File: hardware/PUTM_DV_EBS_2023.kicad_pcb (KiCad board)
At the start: 4 copper layers, 100 x 70 mm, 155 parts, among them IC1 UCC2946DG4, J1 SAFETY_SUPPLY, J2 SWDIO_CONN, J3 SENSORS, J4 VALVES, J5 MAIN, K1 FINDER-30.22, K2 FINDER-30.22, Q1 BSS123, Q2 BSS123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

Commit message: 2.0 layot wip, each sections placed
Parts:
- removed D10: UDZV_3.3B, Diode_SMD:D_SOD-323_HandSoldering
- removed the R11 at (150.6, 42.7)
- removed R25: 2.2k, Resistor_SMD:R_0603_1608Metric_Pad0.98x0.95mm_HandSolder
- removed the R5 at (43.2, 33.5)
- removed the R5 at (59.7, 58.9)
- removed the R7 at (74.3, 77.5)
- added JP2: Jumper_NC_Small, Jumper:SolderJumper-2_P1.3mm_Open_RoundedPad1.0x1.5mm, F.Cu at (124.8, 154.6)
- added JP3: Jumper_NC_Small, Jumper:SolderJumper-2_P1.3mm_Open_RoundedPad1.0x1.5mm, F.Cu at (124.8, 158.1)
- added R5: 100R, Resistor_SMD:R_0603_1608Metric_Pad0.98x0.95mm_HandSolder, F.Cu at (152.2, 116.3)
- 120_JP1: footprint Connector_PinHeader_2.54mm:PinHeader_1x02_P2.54mm_Vertical -> Jumper:SolderJumper-2_P1.3mm_Open_RoundedPad1.0x1.5mm
- R11, R2, R33, R6: value 2.2k -> 100R
- moved C30 145.2 mm to (175.1, 125.1)
- moved D13 142.6 mm to (174.9, 127.0)
- moved R30 141.2 mm to (171.8, 125.1)
- moved C29 135.3 mm to (157.5, 125.3)
- moved D14 133.1 mm to (157.2, 132.2)
- moved D9 133.1 mm to (157.2, 127.3)
- moved R28 131.2 mm to (154.2, 125.3)
- moved R6 130.1 mm to (152.2, 110.2)
- moved R11 127.9 mm to (152.2, 108.7)
- moved R33 126.9 mm to (152.2, 111.8)
- moved R49 121.8 mm to (145.7, 115.1)
- moved R29 121.8 mm to (145.7, 110.1)
- moved R50 121.8 mm to (145.7, 117.6)
- moved R14 116.2 mm to (162.7, 108.2)
- moved R16 116.2 mm to (162.7, 106.7)
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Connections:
- U5 pad 26: SPARE1 -> Net-(JP2-A)
- U5 pad 27: SPARE2 -> Net-(JP3-B)
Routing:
- net SPARE2: track 7.06 -> 0.00 mm, vias 2 -> 0
- net Net-(JP3-B): track 0.00 -> 7.06 mm, vias 0 -> 2
- net SPARE1: track 6.13 -> 0.00 mm
- net Net-(JP2-A): track 0.00 -> 6.13 mm
- net /EBS Logic/SAFETY_IN: track 5.07 -> 0.00 mm
- net /Input Protection/SAFETY_SENSE_P: track 0.00 -> 3.60 mm
- net GND: track 51.0 -> 49.4 mm
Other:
- board text added: "SDC_K_CTRL"
- board text added: "Test points:"
- board text added: "WD_RDY"
- board text removed: "AND2"
- board text removed: "LATCH_CHK"
- board text removed: "NAND1"
- board text removed: "RST_EBS"
- board text removed: "RST_LATCH"
- board text removed: "RTH"
- board text removed: "SDC_K"

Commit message: WIP 1.1 routing
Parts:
- removed the C27 at (140.8, 142.9)
- removed JP3: Jumper_NC_Small, Jumper:SolderJumper-2_P1.3mm_Open_RoundedPad1.0x1.5mm
- removed Q1: BSS123, Package_TO_SOT_SMD:SOT-23
- added JP1: Jumper_NC_Small, Jumper:SolderJumper-2_P1.3mm_Open_RoundedPad1.0x1.5mm, F.Cu at (128.6, 82.8)
- added REF**: PinHeader_2x06_P2.54mm_Vertical, Connector_PinHeader_2.54mm:PinHeader_2x06_P2.54mm_Vertical, F.Cu at (172.8, 75.6)
- R1: value 1k -> 100R
- R20, R4: value 2.2k -> 100R
- moved R49 97.7 mm to (57.3, 73.4)
- moved R29 96.5 mm to (57.3, 71.4)
- moved R50 96.5 mm to (57.3, 78.9)
- moved 120_JP1 86.8 mm to (120.1, 44.2), turned to 0 degrees
- moved R13 84.8 mm to (120.7, 47.1), turned to -90 degrees
- moved JP2 74.4 mm to (128.6, 80.3), turned to 180 degrees
- moved C14 71.3 mm to (120.5, 63.9), turned to -90 degrees
- moved C15 67.6 mm to (118.9, 65.7)
- moved U6 65.8 mm to (115.3, 65.7), turned to 90 degrees
- moved C23 63.0 mm to (147.1, 74.0)
- moved C27 63.0 mm to (151.7, 74.0)
- moved U10 63.0 mm to (154.0, 74.8)
- moved U8 63.0 mm to (144.8, 74.8)
- moved U9 63.0 mm to (149.4, 74.8)
- moved C4 63.0 mm to (142.3, 74.0)
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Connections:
- JP2 pad 1: Net-(JP2-A) -> SPARE2
- JP2 pad 2: SPARE1 -> Net-(JP2-B)
- R11 pad 1: Net-(U5-PB4) -> Net-(U5-PB0)
- R5 pad 1: Net-(U5-PB5) -> Net-(U5-PB1)
- R6 pad 1: Net-(U5-PB6) -> Net-(U5-PB2)
- U5 pad 24: unconnected-(U5-PC4-Pad24) -> Net-(JP1-A)
- U5 pad 25: unconnected-(U5-PC5-Pad25) -> Net-(JP2-B)
- U5 pad 26: Net-(JP2-A) -> Net-(U5-PB0)
- U5 pad 27: Net-(JP3-B) -> Net-(U5-PB1)
- U5 pad 28: unconnected-(U5-PB2-Pad28) -> Net-(U5-PB2)
- U5 pad 56: Net-(U5-PB4) -> unconnected-(U5-PB4-Pad56)
- U5 pad 57: Net-(U5-PB5) -> unconnected-(U5-PB5-Pad57)
- U5 pad 58: Net-(U5-PB6) -> unconnected-(U5-PB6-Pad58)
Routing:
- net EBS_RESET _BUTTON: track 43.5 -> 0.00 mm, vias 4 -> 0
- net /Air pressure sensor control/PRESS4: track 0.00 -> 15.1 mm
- net Net-(Q2-G): track 31.4 -> 18.8 mm
- net /EBS Supervisor/VALVE_2: track 0.00 -> 11.2 mm
- net Net-(Q3-G): track 44.3 -> 34.3 mm
- net +3V3: track 86.3 -> 78.2 mm, vias 32 -> 22
- net Net-(U4--): track 0.00 -> 7.55 mm
- net Net-(U2--): track 0.00 -> 7.55 mm
- net Net-(U1--): track 0.00 -> 7.55 mm
- net Net-(U3--): track 0.00 -> 7.55 mm
- net Net-(JP3-B): track 7.06 -> 0.00 mm, vias 2 -> 0
- net CAN+: track 0.00 -> 6.75 mm
- net Net-(JP2-A): track 6.13 -> 0.00 mm
- net Net-(IC1-Pad2): track 6.03 -> 0.00 mm
- net CAN-: track 0.00 -> 5.96 mm
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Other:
- board text removed: "///// REROUTE AND REPAIR CRYSTAL"
- board text removed: "Power Supply"

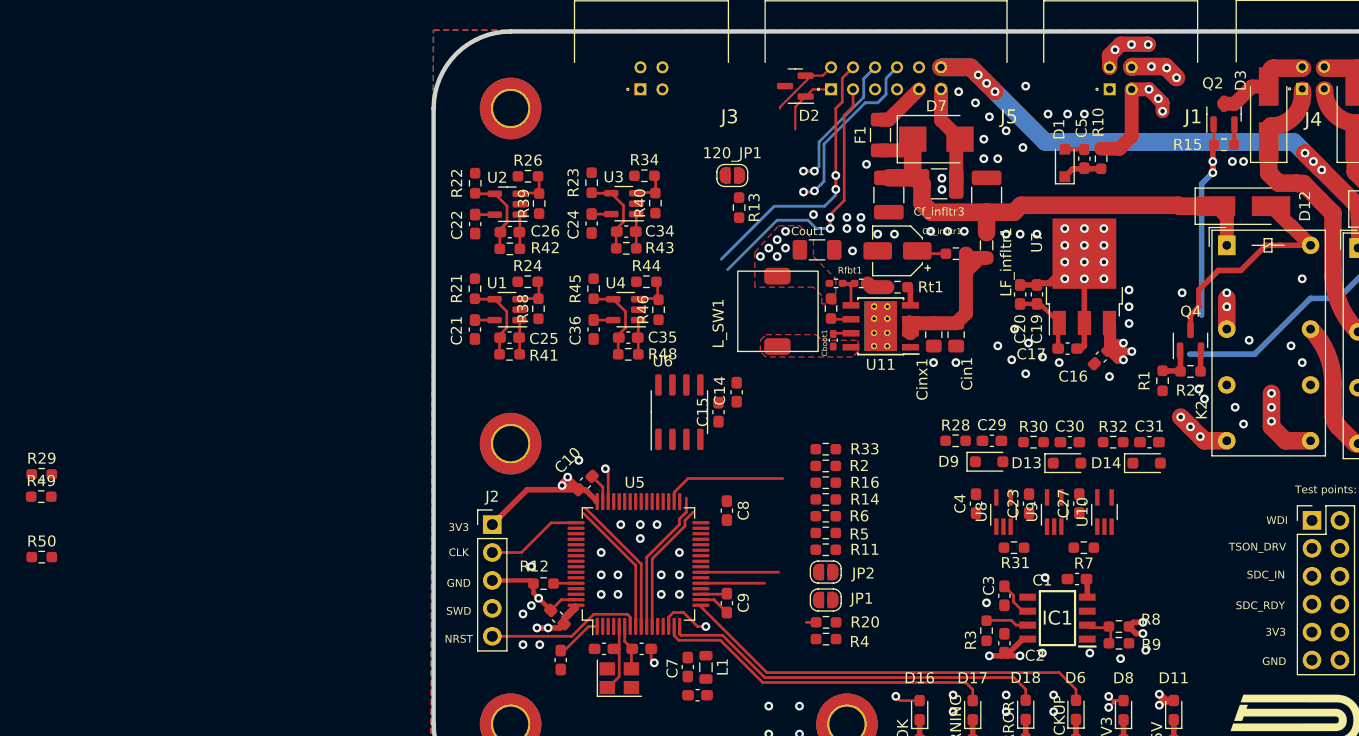
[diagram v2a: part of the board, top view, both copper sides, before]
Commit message: 2.0 layot wip , routing 2
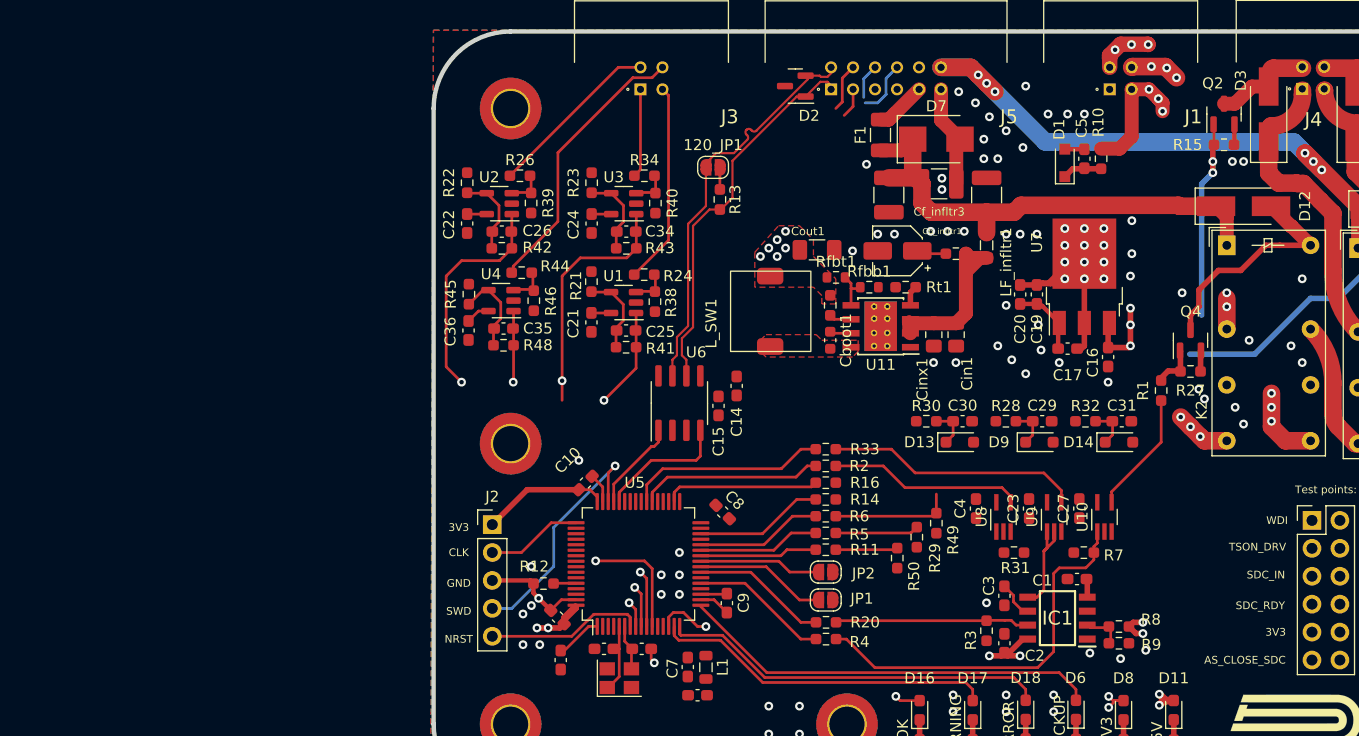
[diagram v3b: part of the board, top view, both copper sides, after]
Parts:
- Cboot1: footprint Capacitor_SMD:C_0402_1005Metric_Pad0.74x0.62mm_HandSolder -> Capacitor_SMD:C_0603_1608Metric
- Rfbb1, Rfbt1: footprint Resistor_SMD:R_0402_1005Metric_Pad0.72x0.64mm_HandSolder -> Resistor_SMD:R_0603_1608Metric
- moved R49 81.4 mm to (138.7, 75.8), turned to -90 degrees
- moved R29 79.8 mm to (136.9, 77.1), turned to -90 degrees
- moved R50 77.8 mm to (135.1, 79.0), turned to -90 degrees
- moved C36 11.4 mm to (96.1, 58.3)
- moved C35 11.4 mm to (99.3, 58.1)
- moved R46 11.4 mm to (102.1, 55.6)
- moved R48 11.4 mm to (99.3, 59.6)
- moved R44 11.4 mm to (101.0, 53.0)
- moved U4 11.4 mm to (99.1, 55.6)
- moved R45 11.4 mm to (96.2, 55.0)
- moved C21 10.6 mm to (107.3, 57.6)
- moved C25 10.6 mm to (110.5, 58.3)
- moved R21 10.6 mm to (107.3, 53.8)
- moved R24 10.6 mm to (112.1, 53.2)
- moved R38 10.6 mm to (113.1, 55.7)
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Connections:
- REF** pad 1: (no net) -> /EBS Supervisor/WATCHDOG
- REF** pad 10: (no net) -> +5V
- REF** pad 11: (no net) -> /EBS Supervisor/AS_CLOSE_SDC
- REF** pad 12: (no net) -> GND
- REF** pad 2: (no net) -> Net-(IC1-~{WDO})
- REF** pad 3: (no net) -> TS_COCKPIT_P
- REF** pad 4: (no net) -> TS_ON_EXT_P
- REF** pad 5: (no net) -> /Input Protection/SAFETY_SENSE_P
- REF** pad 6: (no net) -> /EBS Supervisor/WD_ready
- REF** pad 7: (no net) -> /EBS Supervisor/SDC_READY
- REF** pad 8: (no net) -> /Safety Relay/SAFETY_RELAY
- REF** pad 9: (no net) -> +3V3
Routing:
- net /EBS Supervisor/AS_CLOSE_SDC: track 0.00 -> 35.4 mm
- net /Air pressure sensor control/EBS: track 15.4 -> 50.1 mm, vias 0 -> 2
- net /Air pressure sensor control/REDUNDANT: track 16.0 -> 47.5 mm, vias 0 -> 2
- net CAN+: track 6.75 -> 37.3 mm
- net CAN-: track 5.96 -> 34.7 mm
- net SENSORIN_SPARE: track 0.00 -> 25.4 mm
- net DASH_TS_ON: track 26.0 -> 2.71 mm, vias 2 -> 0
- net /EBS Supervisor/WD_ready: track 0.00 -> 23.2 mm
- net TS_ON_EXTERNAL: track 26.4 -> 4.39 mm, vias 2 -> 0
- net /Air pressure sensor control/PRESS4: track 15.1 -> 37.0 mm, vias 0 -> 2
- net SENSORIN_MAIN: track 0.00 -> 18.4 mm
- net Net-(U5-PC8): track 0.00 -> 18.2 mm
- net /EBS Supervisor/SDC_READY: track 0.00 -> 17.6 mm
- net Net-(U5-PC7): track 0.00 -> 16.7 mm
- net SENSORIN_EBS: track 0.00 -> 16.0 mm
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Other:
- board text added: "AS_CLOSE_SDC"

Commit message: 2.0 layot wip , routing 3
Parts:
- removed J1: SAFETY_SUPPLY, PUTM_Kicad_FOOTPRINTS:M80-5L104YYMC
- removed J3: SENSORS, PUTM_Kicad_FOOTPRINTS:M80-5L104YYMC
- removed J4: VALVES, PUTM_Kicad_FOOTPRINTS:M80-5L104YYMC
- removed J5: MAIN, PUTM_Kicad_FOOTPRINTS:M80-5L112YYMC
- added J6: IDC Connector, Connector_IDC:IDC-Header_2x15-1MP_P2.54mm_Latch6.5mm_Vertical, F.Cu at (124.7, 37.3)
- D12, D3, D4, D5: footprint Diode_SMD:D_SMA_Handsoldering -> Diode_SMD:D_SMA
- moved C5 35.8 mm to (165.1, 76.1)
- moved D1 35.8 mm to (163.3, 76.5)
- moved R10 35.8 mm to (166.6, 76.1)
- moved Q3 13.0 mm to (170.9, 47.0), turned to 180 degrees
- moved D5 10.3 mm to (167.4, 42.9), turned to 180 degrees
- moved D3 10.1 mm to (159.8, 42.9), turned to 180 degrees
- moved D7 9.81 mm to (130.3, 46.0), turned to -90 degrees
- moved R17 9.11 mm to (173.7, 47.0), turned to 90 degrees
- moved Q2 8.86 mm to (162.0, 47.0), turned to 180 degrees
- moved D2 8.71 mm to (124.7, 44.7), turned to -135 degrees
- moved D12 6.01 mm to (170.6, 51.5)
- moved 120_JP1 5.60 mm to (117.6, 49.0)
- moved R15 5.60 mm to (164.7, 47.0), turned to 90 degrees
- moved R13 5.59 mm to (118.2, 51.9)
- moved K2 4.58 mm to (166.6, 54.9)
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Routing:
- net LINE: track 63.4 -> 0.00 mm, vias 6 -> 0
- net TSMS: track 57.5 -> 4.17 mm, vias 6 -> 0
- net +5V: track 104.3 -> 132.6 mm, vias 11 -> 17
- net +24V: track 46.0 -> 18.2 mm
- net +3V3: track 74.7 -> 92.0 mm
- net Net-(D12-A): track 20.9 -> 4.05 mm
- net GND: track 44.1 -> 27.4 mm, vias 110 -> 62
- net TS_ON_EXT_P: track 11.3 -> 26.8 mm, vias 0 -> 2
- net /EBS Supervisor/SDC_READY: track 17.6 -> 32.5 mm, vias 0 -> 2
- net SENSORIN_EBS: track 16.0 -> 28.7 mm
- net SENSORIN_MAIN: track 18.4 -> 30.2 mm
- net Net-(Q2-G): track 18.8 -> 30.3 mm, vias 2 -> 1
- net SENSORIN_REDUNDANT: track 8.09 -> 18.9 mm
- net SAFETY_RESET_BUTT_P: track 9.37 -> 19.5 mm, vias 0 -> 1
- net SAFETY_IN: track 54.4 -> 44.9 mm, vias 6 -> 0
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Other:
- board size 100 x 70 mm -> 97 x 70 mm

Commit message: Dimensions compress, routing
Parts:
- added C12: 100nF, Capacitor_SMD:C_0603_1608Metric_Pad1.08x0.95mm_HandSolder, F.Cu at (66.3, 77.0)
- added C14: 100nF, Capacitor_SMD:C_0603_1608Metric_Pad1.08x0.95mm_HandSolder, F.Cu at (66.4, 58.7)
- added C15: 100nF, Capacitor_SMD:C_0603_1608Metric_Pad1.08x0.95mm_HandSolder, F.Cu at (66.4, 61.2)
- added C18: 1uF, Capacitor_SMD:C_0603_1608Metric_Pad1.08x0.95mm_HandSolder, F.Cu at (122.0, 74.4)
- added C7: 100nF, Capacitor_SMD:C_0603_1608Metric_Pad1.08x0.95mm_HandSolder, F.Cu at (66.3, 67.0)
- added C8: 100nF, Capacitor_SMD:C_0603_1608Metric_Pad1.08x0.95mm_HandSolder, F.Cu at (66.3, 69.5)
- added C9: 100nF, Capacitor_SMD:C_0603_1608Metric_Pad1.08x0.95mm_HandSolder, F.Cu at (66.3, 72.0)
- C6: value 1uF -> 100nF
- R21, R22, R23, R24, R26, R34, R44, R45: value 200k 1% -> 20k 1%
- R38, R39, R40, R41, R42, R43, R46, R48: value 100k 1% -> 10k 1%
- Y1: value Crystal_GND24 -> 8MHz 3225 Crystal
- moved C6 57.4 mm to (66.3, 64.5), turned to 0 degrees
- moved C8 0.28 mm to (119.1, 75.1)
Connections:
- net /EBS Supervisor/(CAN_RX)+ renamed /EBS Supervisor/CAN_RX
- net /EBS Supervisor/(CAN_TX)- renamed /EBS Supervisor/CAN_TX
- net /EBS Supervisor/XTAL1 renamed Net-(U5-PH0-OSC_IN)
- net /EBS Supervisor/XTAL2 renamed Net-(U5-PH1-OSC_OUT)
- C6 pad 1: +3V3 -> /EBS Supervisor/uC power decoupling/3v3_A
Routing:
- net SAFETY_RESET_BUTT_P: track 19.5 -> 37.7 mm, vias 1 -> 2
- net +24V: track 18.2 -> 27.2 mm
- net 24v input: track 0.00 -> 5.62 mm
- net Net-(Q4-G): track 0.00 -> 3.70 mm
- net SAFETY_IN: track 44.9 -> 47.5 mm
- net Net-(Q3-G): track 33.3 -> 35.2 mm
- net Net-(Q2-G): track 30.3 -> 32.1 mm
- net /Air pressure sensor control/REDUNDANT: track 47.5 -> 45.8 mm

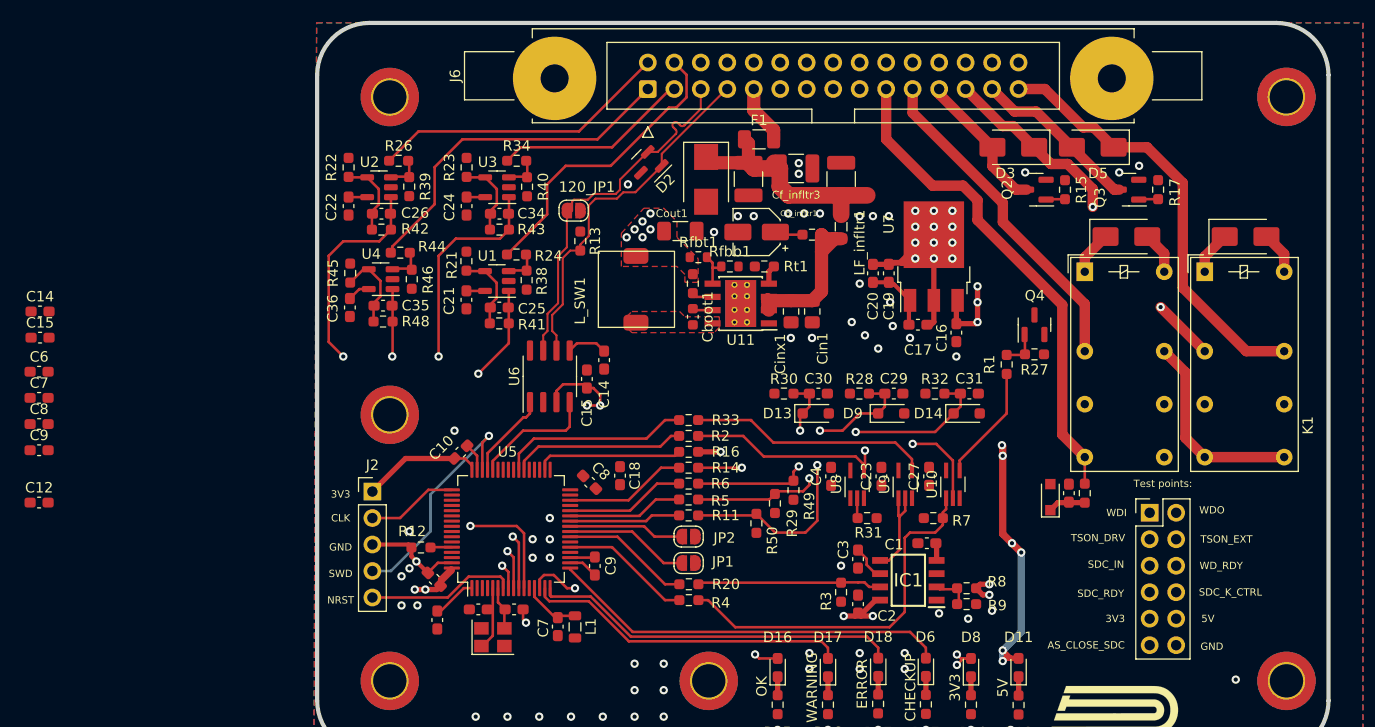
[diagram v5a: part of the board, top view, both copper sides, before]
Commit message: replace RES2 input to actuator relai
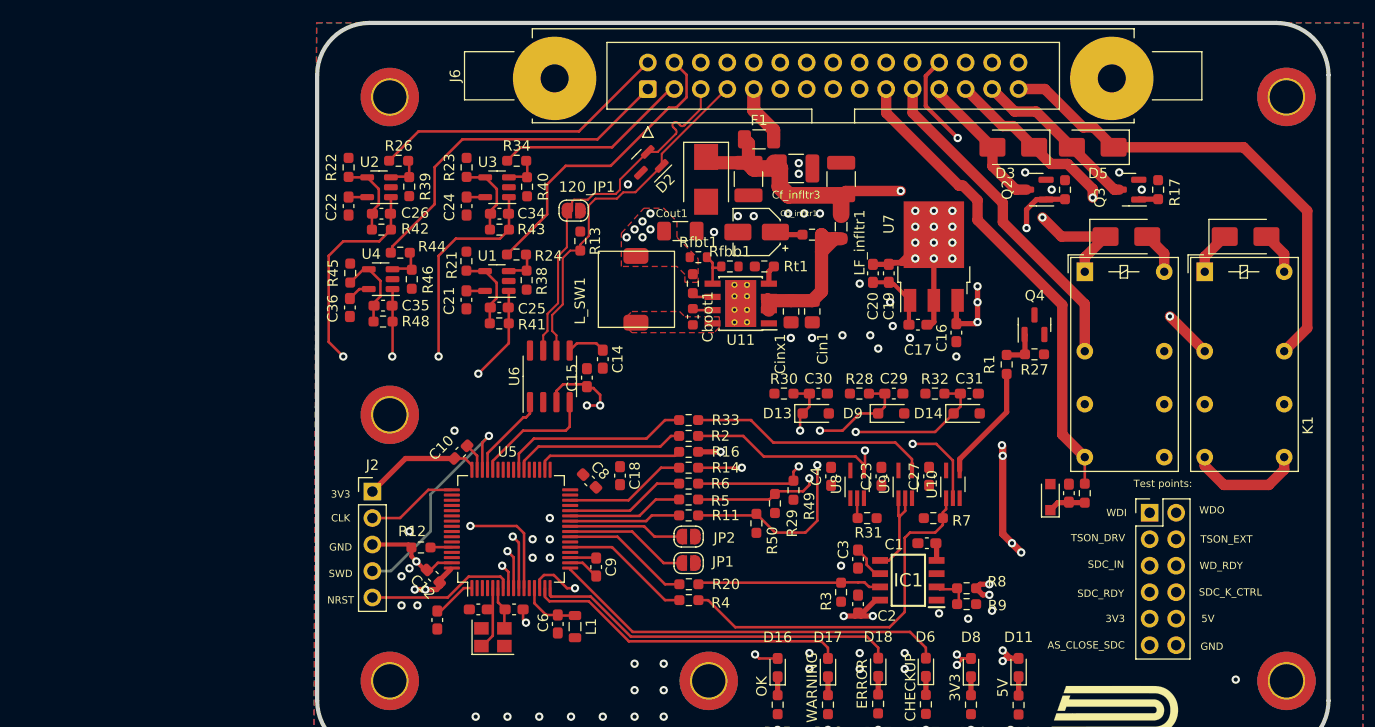
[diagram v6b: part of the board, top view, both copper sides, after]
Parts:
- removed the C12 at (104.2, 84.4)
- removed the C14 at (66.4, 58.7)
- removed the C14 at (120.5, 63.3)
- removed the C15 at (118.9, 65.2)
- removed C7 (x2): 100nF, Capacitor_SMD:C_0603_1608Metric_Pad1.08x0.95mm_HandSolder
- removed the C8 at (119.1, 75.1)
- removed the C9 at (119.6, 83.1)
- added C14: 100nF, Capacitor_SMD:C_0603_1608Metric_Pad1.08x0.95mm_HandSolder, F.Cu at (120.4, 63.2)
- moved C6 55.3 mm to (116.1, 88.6), turned to -90 degrees
- moved C9 54.6 mm to (119.8, 83.2), turned to -90 degrees
- moved C8 53.1 mm to (119.1, 74.9), turned to -45 degrees
- moved C15 52.6 mm to (118.9, 65.0), turned to 90 degrees
- moved C12 38.5 mm to (104.1, 84.1), turned to 135 degrees
- turned L1 to -90 degrees
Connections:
- C6 pad 1: /EBS Supervisor/uC power decoupling/3v3_A -> 3v3_A
- J6 pad 15: EBS_RESET _BUTTON -> TS_ON_EXTERNAL
- J6 pad 17: TS_ON_EXTERNAL -> EBS_RESET _BUTTON
- J6 pad 24: TSMS -> LINE
- J6 pad 26: LINE -> TSMS
- K1 pad 14: /Safety Relay/VALVE_SUPPLY -> LINE
- K1 pad 24: /Safety Relay/VALVE_SUPPLY -> LINE
- K2 pad 21: /Safety Relay/VALVE_SUPPLY -> unconnected-(K2-Pad21)
- K2 pad 24: LINE -> unconnected-(K2-Pad24)
- L1 pad 1: +3V3 -> 3v3_A
- L1 pad 2: /EBS Supervisor/3v3_A -> +3V3
- U5 pad 13: /EBS Supervisor/3v3_A -> 3v3_A
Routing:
- net +24V: track 27.2 -> 52.1 mm, vias 0 -> 2
- net LINE: track 0.00 -> 20.1 mm, vias 0 -> 1
- net /Safety Relay/VALVE_SUPPLY: track 19.4 -> 0.00 mm
- net 3v3_A: track 0.00 -> 5.83 mm
- net /EBS Supervisor/3v3_A: track 5.62 -> 0.00 mm
- net VALVE_2_COIL_I: track 41.8 -> 46.9 mm
- net Net-(Q2-G): track 32.1 -> 36.2 mm, vias 1 -> 2
- net +3V3: track 92.0 -> 90.1 mm
- net SAFETY_IN: track 47.5 -> 46.0 mm
- net GND: vias 62 -> 59
- net (no net): vias 4 -> 5
